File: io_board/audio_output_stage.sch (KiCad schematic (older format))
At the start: 40 parts

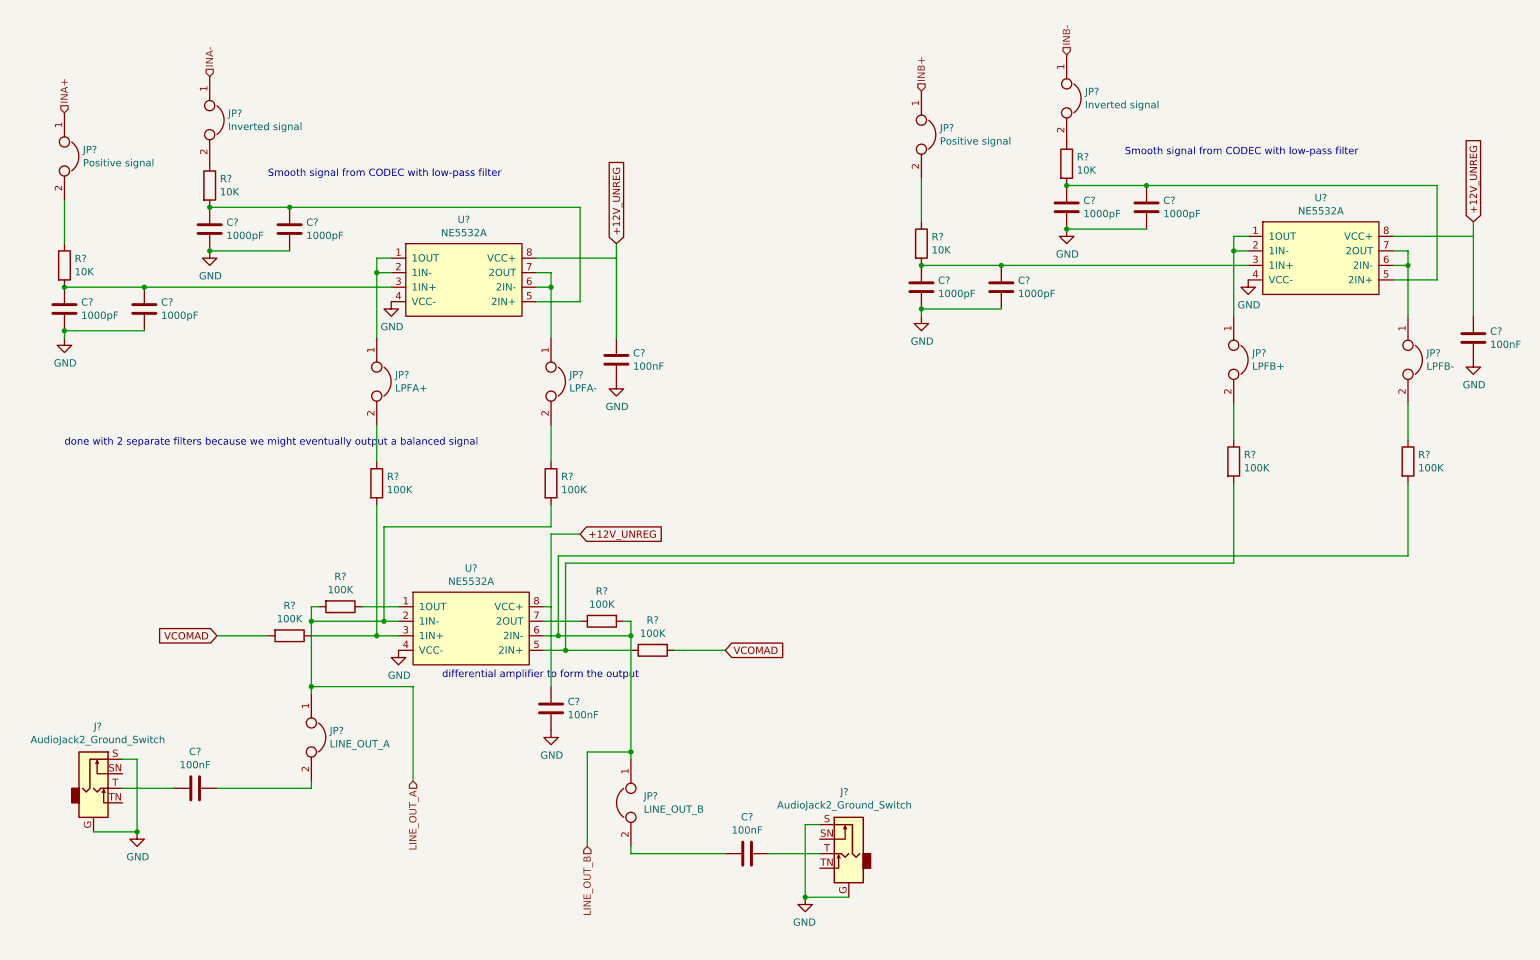
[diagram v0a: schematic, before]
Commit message: Added MIDI connectors and SD card to io_board
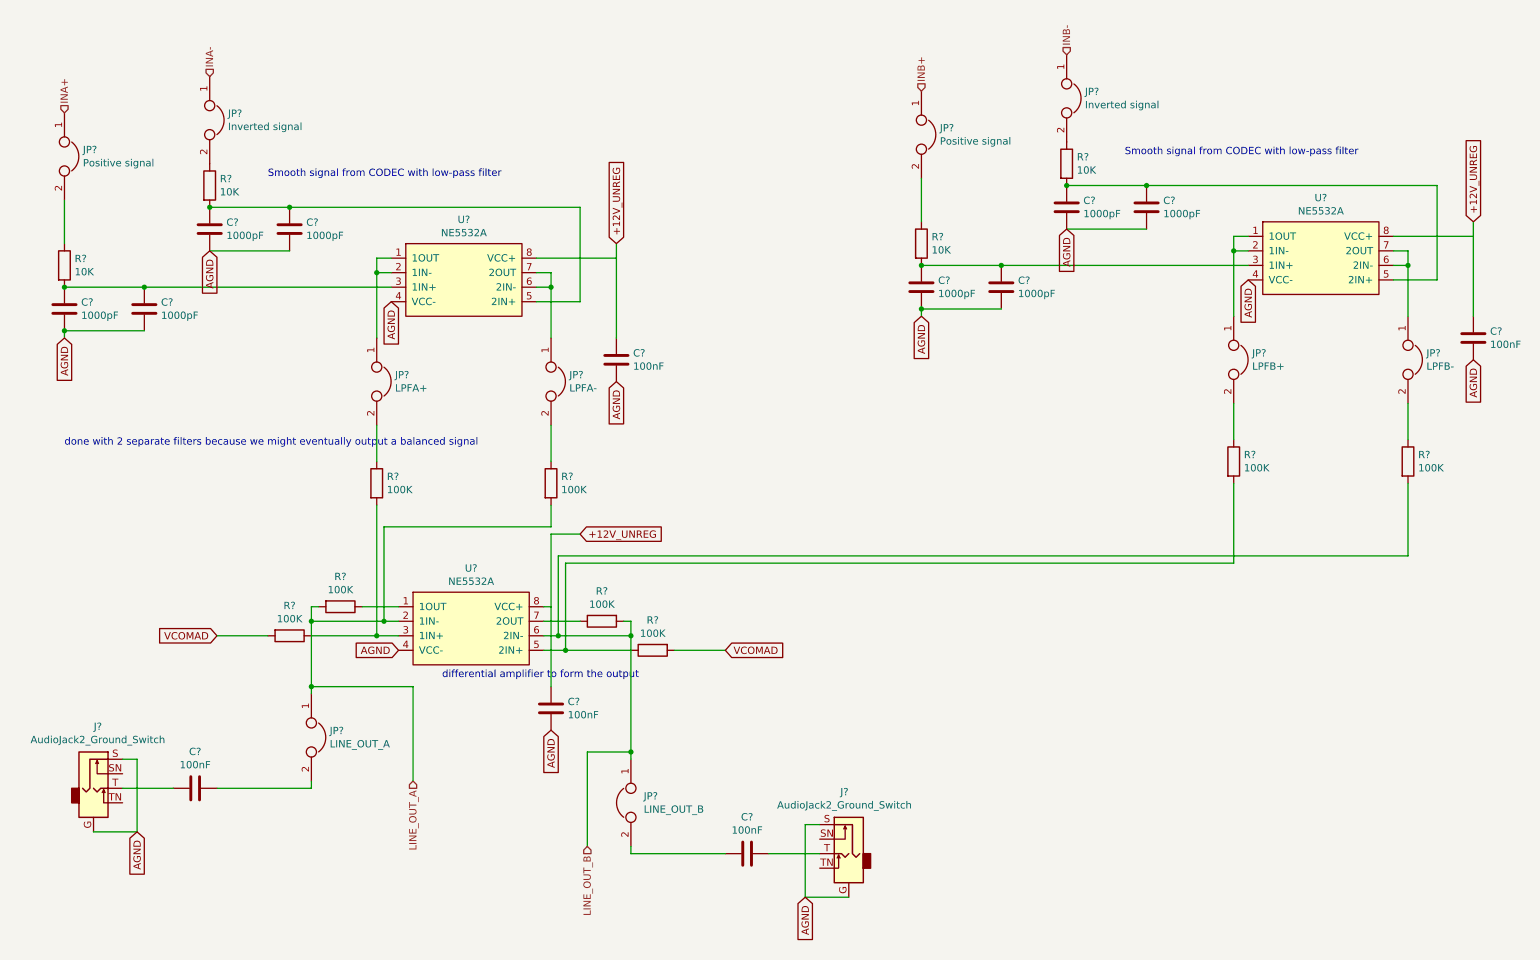
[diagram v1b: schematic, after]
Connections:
- net GND renamed AGND
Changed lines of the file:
@@
 EESchema Schematic File Version 4
 LIBS:io_board-cache
-EELAYER 26 0
+EELAYER 29 0
 EELAYER END
 $Descr A4 11693 8268
 encoding utf-8
-Sheet 4 5
+Sheet 4 8
 Title ""
 Date ""
@@
 	1850 2250 2400 2250
 Connection ~ 1850 2250
-$Comp
-L power:GND #PWR?
-U 1 1 5D3F5A0F
-P 850 3150
-AR Path="/5D3A0EFE/5D3F5A0F" Ref="#PWR?"  Part="1"
-AR Path="/5D3F56F3/5D3F5A0F" Ref="#PWR?"  Part="1"
-F 0 "#PWR?" H 850 2900 50  0001 C CNN
-F 1 "GND" H 855 2977 50  0000 C CNN
-F 2 "" H 850 3150 50  0001 C CNN
-F 3 "" H 850 3150 50  0001 C CNN
-	1    850  3150
-	1    0    0    -1
-$EndComp
 Wire Wire Line
 	850  3150 850  3100
@@
 	1400 3100 850  3100
 Connection ~ 850  3100
-$Comp
-L power:GND #PWR?
-U 1 1 5D3F5A18
-P 1850 2550
-AR Path="/5D3A0EFE/5D3F5A18" Ref="#PWR?"  Part="1"
-AR Path="/5D3F56F3/5D3F5A18" Ref="#PWR?"  Part="1"
-F 0 "#PWR?" H 1850 2300 50  0001 C CNN
-F 1 "GND" H 1855 2377 50  0000 C CNN
-F 2 "" H 1850 2550 50  0001 C CNN
-F 3 "" H 1850 2550 50  0001 C CNN
-	1    1850 2550
-	1    0    0    -1
-$EndComp
 Wire Wire Line
 	1850 2550 2400 2550
-Connection ~ 1850 2550
 Wire Wire Line
 	1400 2800 850  2800
@@
 Wire Wire Line
 	4200 2800 4100 2800
-$Comp
-L power:GND #PWR?
-U 1 1 5D3F5FE2
-P 3100 2900
-AR Path="/5D3A0EFE/5D3F5FE2" Ref="#PWR?"  Part="1"
-AR Path="/5D3F56F3/5D3F5FE2" Ref="#PWR?"  Part="1"
-F 0 "#PWR?" H 3100 2650 50  0001 C CNN
-F 1 "GND" H 3105 2727 50  0000 C CNN
-F 2 "" H 3100 2900 50  0001 C CNN
-F 3 "" H 3100 2900 50  0001 C CNN
-	1    3100 2900
-	1    0    0    -1
-$EndComp
 Text GLabel 4650 2500 1    50   Input ~ 0
 +12V_UNREG
@@
 Wire Wire Line
 	3050 5100 3150 5100
-$Comp
-L power:GND #PWR?
-U 1 1 5D3F916A
-P 3150 5300
-AR Path="/5D3A0EFE/5D3F916A" Ref="#PWR?"  Part="1"
-AR Path="/5D3F56F3/5D3F916A" Ref="#PWR?"  Part="1"
-F 0 "#PWR?" H 3150 5050 50  0001 C CNN
-F 1 "GND" H 3155 5127 50  0000 C CNN
-F 2 "" H 3150 5300 50  0001 C CNN
-F 3 "" H 3150 5300 50  0001 C CNN
-	1    3150 5300
-	1    0    0    -1
-$EndComp
 Text GLabel 4400 4500 2    50   Input ~ 0
 +12V_UNREG
@@
 Wire Wire Line
 	2550 6250 1900 6250
-$Comp
-L power:GND #PWR?
-U 1 1 5D3FE2B7
-P 1350 6550
-F 0 "#PWR?" H 1350 6300 50  0001 C CNN
-F 1 "GND" H 1355 6377 50  0000 C CNN
-F 2 "" H 1350 6550 50  0001 C CNN
-F 3 "" H 1350 6550 50  0001 C CNN
-	1    1350 6550
-	1    0    0    -1
-$EndComp
 Wire Wire Line
 	1250 6050 1350 6050
@@
 Wire Wire Line
 	1350 6050 1350 6550
-Connection ~ 1350 6550
 Text HLabel 3250 6200 3    50   Input ~ 0
 LINE_OUT_A
@@
 	7750 2100 8300 2100
 Connection ~ 7750 2100
-$Comp
-L power:GND #PWR?
-U 1 1 5D4049E9
-P 6750 3000
-AR Path="/5D3A0EFE/5D4049E9" Ref="#PWR?"  Part="1"
-AR Path="/5D3F56F3/5D4049E9" Ref="#PWR?"  Part="1"
-F 0 "#PWR?" H 6750 2750 50  0001 C CNN
-F 1 "GND" H 6755 2827 50  0000 C CNN
-F 2 "" H 6750 3000 50  0001 C CNN
-F 3 "" H 6750 3000 50  0001 C CNN
-	1    6750 3000
-	1    0    0    -1
-$EndComp
 Wire Wire Line
 	6750 3000 6750 2950
@@
 	7300 2950 6750 2950
 Connection ~ 6750 2950
-$Comp
-L power:GND #PWR?
-U 1 1 5D4049F2
-P 7750 2400
-AR Path="/5D3A0EFE/5D4049F2" Ref="#PWR?"  Part="1"
-AR Path="/5D3F56F3/5D4049F2" Ref="#PWR?"  Part="1"
-F 0 "#PWR?" H 7750 2150 50  0001 C CNN
-F 1 "GND" H 7755 2227 50  0000 C CNN
-F 2 "" H 7750 2400 50  0001 C CNN
-F 3 "" H 7750 2400 50  0001 C CNN
-	1    7750 2400
-	1    0    0    -1
-$EndComp
 Wire Wire Line
 	7750 2400 8300 2400
-Connection ~ 7750 2400
 Wire Wire Line
 	7300 2650 6750 2650
@@
 Wire Wire Line
 	10100 2650 10000 2650
-$Comp
-L power:GND #PWR?
-U 1 1 5D404A1B
-P 9000 2750
-AR Path="/5D3A0EFE/5D404A1B" Ref="#PWR?"  Part="1"
-AR Path="/5D3F56F3/5D404A1B" Ref="#PWR?"  Part="1"
-F 0 "#PWR?" H 9000 2500 50  0001 C CNN
-F 1 "GND" H 9005 2577 50  0000 C CNN
-F 2 "" H 9000 2750 50  0001 C CNN
-F 3 "" H 9000 2750 50  0001 C CNN
-	1    9000 2750
-	1    0    0    -1
-$EndComp
 Text GLabel 10550 2350 1    50   Input ~ 0
 +12V_UNREG
@@
 Wire Wire Line
 	4750 6700 5400 6700
-$Comp
-L power:GND #PWR?
-U 1 1 5D4105E9
-P 5950 7000
-F 0 "#PWR?" H 5950 6750 50  0001 C CNN
-F 1 "GND" H 5955 6827 50  0000 C CNN
-F 2 "" H 5950 7000 50  0001 C CNN
-F 3 "" H 5950 7000 50  0001 C CNN
-	1    5950 7000
-	-1   0    0    -1
-$EndComp
 Wire Wire Line
 	6050 6500 5950 6500
@@
 Wire Wire Line
 	5950 6500 5950 7000
-Connection ~ 5950 7000
 Text HLabel 4450 6650 3    50   Input ~ 0
 LINE_OUT_B
@@
 	4650 2600 4650 3150
 $Comp
-L power:GND #PWR?
-U 1 1 5D4322C8
-P 4650 3450
-F 0 "#PWR?" H 4650 3200 50  0001 C CNN
-F 1 "GND" H 4655 3277 50  0000 C CNN
-F 2 "" H 4650 3450 50  0001 C CNN
-F 3 "" H 4650 3450 50  0001 C CNN
-	1    4650 3450
-	1    0    0    -1
-$EndComp
-$Comp
 L Device:C C?
 U 1 1 5D434729
@@
 	10550 2450 10550 3000
 $Comp
-L power:GND #PWR?
-U 1 1 5D434731
-P 10550 3300
-F 0 "#PWR?" H 10550 3050 50  0001 C CNN
-F 1 "GND" H 10555 3127 50  0000 C CNN
-F 2 "" H 10550 3300 50  0001 C CNN
-F 3 "" H 10550 3300 50  0001 C CNN
-	1    10550 3300
-	1    0    0    -1
-$EndComp
-$Comp
 L Device:C C?
 U 1 1 5D4391B4
@@
 Wire Wire Line
 	4200 5000 4200 5550
-$Comp
-L power:GND #PWR?
-U 1 1 5D4391BC
-P 4200 5850
-F 0 "#PWR?" H 4200 5600 50  0001 C CNN
-F 1 "GND" H 4205 5677 50  0000 C CNN
-F 2 "" H 4200 5850 50  0001 C CNN
-F 3 "" H 4200 5850 50  0001 C CNN
-	1    4200 5850
-	1    0    0    -1
-$EndComp
 Wire Wire Line
 	2550 5100 2550 5550
 Wire Wire Line
 	4750 5200 4750 6000
+Text GLabel 850  3150 3    50   Input ~ 0
+AGND
+Text GLabel 1850 2550 3    50   Input ~ 0
+AGND
+Text GLabel 3100 2900 3    50   Input ~ 0
+AGND
+Text GLabel 6750 3000 3    50   Input ~ 0
+AGND
+Text GLabel 4650 3450 3    50   Input ~ 0
+AGND
+Text GLabel 1350 6550 3    50   Input ~ 0
+AGND
+Text GLabel 3150 5300 0    50   Input ~ 0
+AGND
+Text GLabel 4200 5850 3    50   Input ~ 0
+AGND
+Text GLabel 5950 7000 3    50   Input ~ 0
+AGND
+Text GLabel 7750 2400 3    50   Input ~ 0
+AGND
+Text GLabel 9000 2750 3    50   Input ~ 0
+AGND
+Text GLabel 10550 3300 3    50   Input ~ 0
+AGND
 $EndSCHEMATC
